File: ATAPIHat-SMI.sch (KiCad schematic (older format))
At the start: 37 parts, among them J1 Pi, J2 IDE

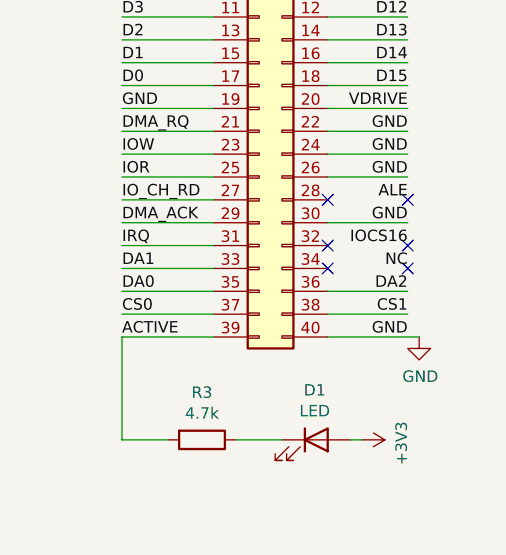
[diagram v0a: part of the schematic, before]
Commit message: Correct cable select
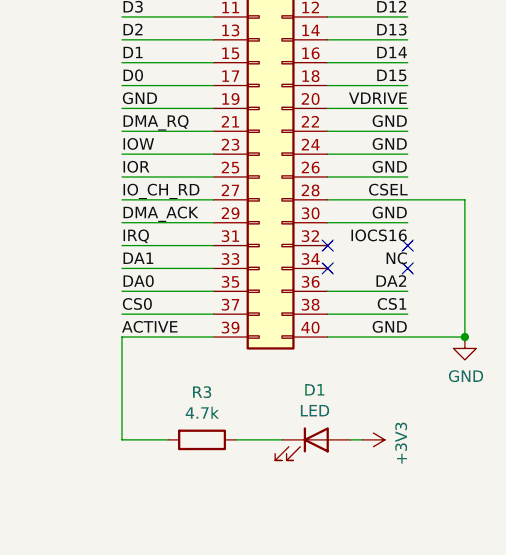
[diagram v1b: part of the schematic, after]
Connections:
- net GND: now also J2.28 (Pin_28)
- no-connect marks 6 -> 4
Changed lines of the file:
@@
 Text Label 9450 4250 2    50   ~ 0
 GND
-Text Label 9450 4150 2    50   ~ 0
-ALE
 Text Label 9450 4050 2    50   ~ 0
 GND
@@
 NoConn ~ 9100 4350
 NoConn ~ 9450 4350
-NoConn ~ 9100 4150
-NoConn ~ 9450 4150
 $Comp
 L Device:LED D1
@@
 L power:GND #PWR0114
 U 1 1 5F25F1E2
-P 9500 4750
-F 0 "#PWR0114" H 9500 4500 50  0001 C CNN
-F 1 "GND" H 9505 4577 50  0000 C CNN
-F 2 "" H 9500 4750 50  0001 C CNN
-F 3 "" H 9500 4750 50  0001 C CNN
-	1    9500 4750
-	1    0    0    -1
-$EndComp
-Wire Wire Line
-	9100 4750 9500 4750
+P 9700 4750
+F 0 "#PWR0114" H 9700 4500 50  0001 C CNN
+F 1 "GND" H 9705 4577 50  0000 C CNN
+F 2 "" H 9700 4750 50  0001 C CNN
+F 3 "" H 9700 4750 50  0001 C CNN
+	1    9700 4750
+	1    0    0    -1
+$EndComp
 Wire Wire Line
 	8200 4250 8600 4250
@@
 Wire Wire Line
 	3200 3250 3600 3250
+Text Label 9450 4150 2    50   ~ 0
+CSEL
+Wire Wire Line
+	9700 4150 9700 4750
+Wire Wire Line
+	9100 4150 9700 4150
+Connection ~ 9700 4750
+Wire Wire Line
+	9100 4750 9700 4750
 $EndSCHEMATC

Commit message: Do layout
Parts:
- added C1: 100nF, Capacitor_SMD:C_0402_1005Metric, symbol Device:C
- added C2: 22uF, Capacitor_SMD:C_0805_2012Metric, symbol Device:C
- gave numbers to parts that had none: 33
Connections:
- net +3V3: now also C1.1
- net ACTIVE: now also R3.1; no longer R3.2
- net GND: now also C1.2, C2.2
- net VDRIVE: now also C2.1
- net at D1.1 (K): now also R3.2; no longer R3.1
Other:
- moved on the sheet: D1, R3

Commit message: Add tooling holes
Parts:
- added H? (x2): ToolingHole, ToolingHole:ToolingHole_JLCSMT, symbol Mechanical:MountingHole
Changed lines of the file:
@@
 	8850 4250 8850 4300
 Connection ~ 8850 4300
+$Comp
+L Mechanical:MountingHole H?
+U 1 1 5F423852
+P 9600 800
+F 0 "H?" H 9700 846 50  0000 L CNN
+F 1 "ToolingHole" H 9700 755 50  0000 L CNN
+F 2 "ToolingHole:ToolingHole_JLCSMT" H 9600 800 50  0001 C CNN
+F 3 "~" H 9600 800 50  0001 C CNN
+	1    9600 800
+	1    0    0    -1
+$EndComp
+$Comp
+L Mechanical:MountingHole H?
+U 1 1 5F4243FA
+P 10350 800
+F 0 "H?" H 10450 846 50  0000 L CNN
+F 1 "ToolingHole" H 10450 755 50  0000 L CNN
+F 2 "ToolingHole:ToolingHole_JLCSMT" H 10350 800 50  0001 C CNN
+F 3 "~" H 10350 800 50  0001 C CNN
+	1    10350 800
+	1    0    0    -1
+$EndComp
 $EndSCHEMATC
